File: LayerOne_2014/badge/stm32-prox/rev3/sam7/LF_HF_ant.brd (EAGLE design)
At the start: 99 x 50 mm, 26 parts

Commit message: 
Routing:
- net N$4: track 123.8 -> 138.2 mm
- net LO2: track 54.7 -> 67.1 mm
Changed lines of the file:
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@@
 <layer number="17" name="Pads" color="2" fill="1" visible="yes" active="yes"/>
 <layer number="18" name="Vias" color="2" fill="1" visible="yes" active="yes"/>
-<layer number="19" name="Unrouted" color="6" fill="1" visible="no" active="yes"/>
+<layer number="19" name="Unrouted" color="6" fill="1" visible="yes" active="yes"/>
 <layer number="20" name="Dimension" color="15" fill="1" visible="yes" active="yes"/>
 <layer number="21" name="tPlace" color="7" fill="1" visible="yes" active="yes"/>
@@
 <contactref element="USB1" pad="2"/>
 <wire x1="31.456" y1="9.652" x2="31.536" y2="9.572" width="0.8128" layer="1"/>
-<wire x1="31.536" y1="9.572" x2="31.536" y2="6.652" width="0.8128" layer="1"/>
+<wire x1="31.536" y1="9.572" x2="31.536" y2="6.652" width="1.2192" layer="1"/>
 <wire x1="18.272" y1="12.432" x2="18.288" y2="12.416" width="0.8128" layer="1"/>
 <wire x1="18.288" y1="12.416" x2="18.288" y2="11.938" width="0.8128" layer="1"/>
@@
 <wire x1="21.288" y1="6.652" x2="31.536" y2="6.652" width="0.8128" layer="1"/>
 <wire x1="31.536" y1="12.462" x2="31.456" y2="12.382" width="0.8128" layer="1"/>
-<wire x1="31.456" y1="12.382" x2="31.456" y2="9.652" width="0.8128" layer="1"/>
+<wire x1="31.456" y1="12.382" x2="31.456" y2="9.652" width="1.2192" layer="1"/>
 <wire x1="6.604" y1="17.78" x2="8.382" y2="19.558" width="0.8128" layer="1"/>
 <wire x1="8.382" y1="19.558" x2="15.748" y2="19.558" width="0.8128" layer="1"/>
@@
 <wire x1="18.288" y1="17.018" x2="18.288" y2="11.938" width="0.8128" layer="1"/>
 <wire x1="31.536" y1="6.652" x2="31.496" y2="6.612" width="0.8128" layer="1"/>
-<wire x1="31.496" y1="6.612" x2="31.496" y2="5.08" width="0.8128" layer="1"/>
-<wire x1="31.496" y1="5.08" x2="32.034" y2="4.542" width="0.8128" layer="1"/>
-<wire x1="32.034" y1="4.542" x2="38.716" y2="4.542" width="0.8128" layer="1"/>
+<wire x1="31.496" y1="6.612" x2="31.496" y2="5.08" width="1.2192" layer="1"/>
+<wire x1="31.496" y1="5.08" x2="32.034" y2="4.542" width="1.2192" layer="1"/>
+<wire x1="32.034" y1="4.542" x2="38.716" y2="4.542" width="1.2192" layer="1"/>
 <wire x1="8.128" y1="3.556" x2="12.954" y2="-1.27" width="0.8128" layer="1"/>
 <wire x1="12.954" y1="-1.27" x2="12.954" y2="-4.826" width="0.8128" layer="1"/>
@@
 <contactref element="USB1" pad="1"/>
 <wire x1="31.456" y1="21.272" x2="31.536" y2="21.192" width="0.8128" layer="1"/>
-<wire x1="31.536" y1="21.192" x2="31.536" y2="18.272" width="0.8128" layer="1"/>
+<wire x1="31.536" y1="21.192" x2="31.536" y2="18.272" width="1.2192" layer="1"/>
 <wire x1="31.536" y1="18.272" x2="31.456" y2="18.192" width="0.8128" layer="1"/>
-<wire x1="31.456" y1="18.192" x2="31.456" y2="15.462" width="0.8128" layer="1"/>
+<wire x1="31.456" y1="18.192" x2="31.456" y2="15.462" width="1.2192" layer="1"/>
 <wire x1="31.456" y1="21.272" x2="31.266" y2="21.082" width="0.8128" layer="1"/>
-<wire x1="31.266" y1="21.082" x2="23.622" y2="21.082" width="0.8128" layer="1"/>
-<wire x1="23.622" y1="21.082" x2="20.772" y2="18.232" width="0.8128" layer="1"/>
-<wire x1="20.772" y1="18.232" x2="20.772" y2="18.034" width="0.8128" layer="1"/>
 <wire x1="20.772" y1="18.034" x2="20.772" y2="12.432" width="0.8128" layer="1"/>
 <wire x1="4.191" y1="7.051040625" x2="4.064" y2="7.178040625" width="0.8128" layer="16"/>
@@
 <wire x1="15.748" y1="21.844" x2="16.962" y2="21.844" width="0.8128" layer="1"/>
 <wire x1="16.962" y1="21.844" x2="20.772" y2="18.034" width="0.8128" layer="1"/>
+<wire x1="31.266" y1="21.082" x2="29.972" y2="21.082" width="0.8128" layer="1"/>
+<wire x1="29.972" y1="21.082" x2="28.194" y2="19.304" width="0.8128" layer="1"/>
+<wire x1="28.194" y1="19.304" x2="28.194" y2="12.954" width="0.8128" layer="1"/>
+<wire x1="28.194" y1="12.954" x2="28.194" y2="12.446" width="0.8128" layer="1"/>
+<wire x1="20.772" y1="12.432" x2="20.772" y2="9.962" width="0.8128" layer="1"/>
+<wire x1="20.772" y1="9.962" x2="21.59" y2="9.144" width="0.8128" layer="1"/>
+<wire x1="21.59" y1="9.144" x2="27.432" y2="9.144" width="0.8128" layer="1"/>
+<wire x1="27.432" y1="9.144" x2="28.194" y2="9.906" width="0.8128" layer="1"/>
+<wire x1="28.194" y1="9.906" x2="28.194" y2="12.954" width="0.8128" layer="1"/>
 </signal>
 <signal name="N$3">
@@
 <wire x1="34.336" y1="6.652" x2="34.336" y2="6.002" width="0.4064" layer="1"/>
 <wire x1="34.256" y1="15.462" x2="34.416" y2="15.622" width="0.8128" layer="1"/>
-<wire x1="34.416" y1="15.622" x2="38.716" y2="15.622" width="0.8128" layer="1"/>
+<wire x1="34.416" y1="15.622" x2="38.716" y2="15.622" width="1.2192" layer="1"/>
 <wire x1="34.336" y1="12.462" x2="34.256" y2="12.382" width="0.8128" layer="1"/>
-<wire x1="34.256" y1="12.382" x2="34.256" y2="9.652" width="0.8128" layer="1"/>
+<wire x1="34.256" y1="12.382" x2="34.256" y2="9.652" width="1.2192" layer="1"/>
 <wire x1="34.256" y1="9.652" x2="34.336" y2="9.572" width="0.8128" layer="1"/>
-<wire x1="34.336" y1="9.572" x2="34.336" y2="6.652" width="0.8128" layer="1"/>
+<wire x1="34.336" y1="9.572" x2="34.336" y2="6.652" width="1.2192" layer="1"/>
 <wire x1="34.256" y1="21.272" x2="34.336" y2="21.192" width="0.8128" layer="1"/>
-<wire x1="34.336" y1="21.192" x2="34.336" y2="18.272" width="0.8128" layer="1"/>
+<wire x1="34.336" y1="21.192" x2="34.336" y2="18.272" width="1.2192" layer="1"/>
 <wire x1="34.336" y1="18.272" x2="34.256" y2="18.192" width="0.8128" layer="1"/>
-<wire x1="34.256" y1="18.192" x2="34.256" y2="15.462" width="0.8128" layer="1"/>
+<wire x1="34.256" y1="18.192" x2="34.256" y2="15.462" width="1.2192" layer="1"/>
 <wire x1="34.256" y1="15.462" x2="34.336" y2="15.382" width="0.8128" layer="1"/>
-<wire x1="34.336" y1="15.382" x2="34.336" y2="12.462" width="0.8128" layer="1"/>
+<wire x1="34.336" y1="15.382" x2="34.336" y2="12.462" width="1.2192" layer="1"/>
 </signal>
 <signal name="N$4">
@@
 <contactref element="USB1" pad="4"/>
 <contactref element="JP1" pad="1"/>
-<wire x1="77.398" y1="-3.4" x2="80.398" y2="-3.4" width="0.8128" layer="1"/>
-<wire x1="80.398" y1="-3.4" x2="80.398" y2="-6.6" width="0.8128" layer="1"/>
-<wire x1="80.398" y1="-6.6" x2="77.398" y2="-6.6" width="0.8128" layer="1"/>
+<wire x1="77.398" y1="-3.4" x2="80.398" y2="-3.4" width="1.2192" layer="1"/>
+<wire x1="80.398" y1="-3.4" x2="80.398" y2="-6.6" width="1.2192" layer="1"/>
+<wire x1="80.398" y1="-6.6" x2="77.398" y2="-6.6" width="1.2192" layer="1"/>
 <wire x1="77.3" y1="-3.302" x2="77.398" y2="-3.4" width="0.8128" layer="1"/>
-<wire x1="9.144" y1="-3.048" x2="13.716" y2="1.524" width="0.8128" layer="16"/>
-<via x="13.716" y="1.524" extent="1-16" drill="0.5"/>
-<wire x1="13.716" y1="1.524" x2="13.772" y2="1.58" width="0.8128" layer="1"/>
 <wire x1="85.948" y1="-15" x2="85.934" y2="-14.986" width="0.6096" layer="1"/>
 <wire x1="78.5" y1="-15" x2="85.948" y2="-15" width="0.6096" layer="1"/>
-<wire x1="13.772" y1="12.432" x2="13.716" y2="12.376" width="0.8128" layer="1"/>
-<wire x1="13.716" y1="12.376" x2="13.716" y2="1.524" width="0.8128" layer="1"/>
 <wire x1="13.772" y1="1.58" x2="30.338" y2="-14.986" width="0.8128" layer="1"/>
 <wire x1="30.338" y1="-14.986" x2="64.262" y2="-14.986" width="0.8128" layer="1"/>
@@
 <wire x1="78.5" y1="-15" x2="64.276" y2="-15" width="0.6096" layer="1"/>
 <wire x1="64.276" y1="-15" x2="64.262" y2="-14.986" width="0.7112" layer="1" curve="-90"/>
+<wire x1="13.772" y1="1.58" x2="13.772" y2="12.432" width="0.8128" layer="1"/>
+<wire x1="9.144" y1="-3.048" x2="9.144" y2="0" width="0.8128" layer="16"/>
+<wire x1="9.144" y1="0" x2="11.43" y2="2.286" width="0.8128" layer="16"/>
+<wire x1="11.43" y1="2.286" x2="11.43" y2="10.922" width="0.8128" layer="16"/>
+<wire x1="11.43" y1="10.922" x2="11.43" y2="11.938" width="0.8128" layer="16"/>
+<wire x1="11.43" y1="11.938" x2="13.716" y2="14.224" width="0.8128" layer="16"/>
+<via x="13.716" y="14.224" extent="1-16" drill="0.5"/>
+<wire x1="13.716" y1="14.224" x2="13.772" y2="14.168" width="0.8128" layer="1"/>
+<wire x1="13.772" y1="14.168" x2="13.772" y2="12.432" width="0.8128" layer="1"/>
 </signal>
 <signal name="HF2">
@@
 <contactref element="TP8" pad="TP"/>
 <wire x1="83.598" y1="-9.4" x2="83.998" y2="-9" width="0.4064" layer="1"/>
-<wire x1="77.398" y1="-9.4" x2="80.398" y2="-9.4" width="0.8128" layer="1"/>
+<wire x1="77.398" y1="-9.4" x2="80.398" y2="-9.4" width="1.2192" layer="1"/>
 <wire x1="80.398" y1="-9.4" x2="83.598" y2="-9.4" width="0.8128" layer="1"/>
 <wire x1="83.598" y1="-9.4" x2="83.998" y2="-9" width="0.8128" layer="1"/>
-<wire x1="83.998" y1="-9" x2="83.998" y2="-12" width="0.8128" layer="1"/>
-<wire x1="83.998" y1="-9" x2="83.998" y2="-5.4" width="0.8128" layer="1"/>
-<wire x1="83.998" y1="-5.4" x2="84.398" y2="-5" width="0.8128" layer="1"/>
+<wire x1="83.998" y1="-9" x2="83.998" y2="-12" width="1.2192" layer="1"/>
+<wire x1="83.998" y1="-9" x2="83.998" y2="-5.4" width="1.2192" layer="1"/>
+<wire x1="83.998" y1="-5.4" x2="84.398" y2="-5" width="1.2192" layer="1"/>
 </signal>
 <signal name="N$5">
@@
 <contactref element="C9" pad="1"/>
 <contactref element="JP1" pad="2"/>
-<wire x1="86.798" y1="-9" x2="86.798" y2="-12" width="0.8128" layer="1"/>
+<wire x1="86.798" y1="-9" x2="86.798" y2="-12" width="1.2192" layer="1"/>
 <wire x1="86.848" y1="-15" x2="86.868" y2="-15" width="0.4064" layer="1"/>
 <wire x1="86.868" y1="-15" x2="86.868" y2="-12.7" width="0.6096" layer="1"/>
@@
 <contactref element="TP7" pad="TP"/>
 <contactref element="USB1" pad="3"/>
-<wire x1="77.398" y1="-0.6" x2="80.398" y2="-0.6" width="0.8128" layer="1"/>
-<wire x1="80.398" y1="-0.6" x2="83.998" y2="-0.6" width="0.8128" layer="1"/>
-<wire x1="83.998" y1="-0.6" x2="84.398" y2="-1" width="0.8128" layer="1"/>
+<wire x1="77.398" y1="-0.6" x2="80.398" y2="-0.6" width="1.2192" layer="1"/>
+<wire x1="80.398" y1="-0.6" x2="83.998" y2="-0.6" width="1.2192" layer="1"/>
+<wire x1="83.998" y1="-0.6" x2="84.398" y2="-1" width="1.2192" layer="1"/>
 <wire x1="77.306" y1="-0.508" x2="77.398" y2="-0.6" width="0.8128" layer="1"/>
 <wire x1="9.144" y1="7.051040625" x2="9.144" y2="11.938" width="0.8128" layer="16"/>

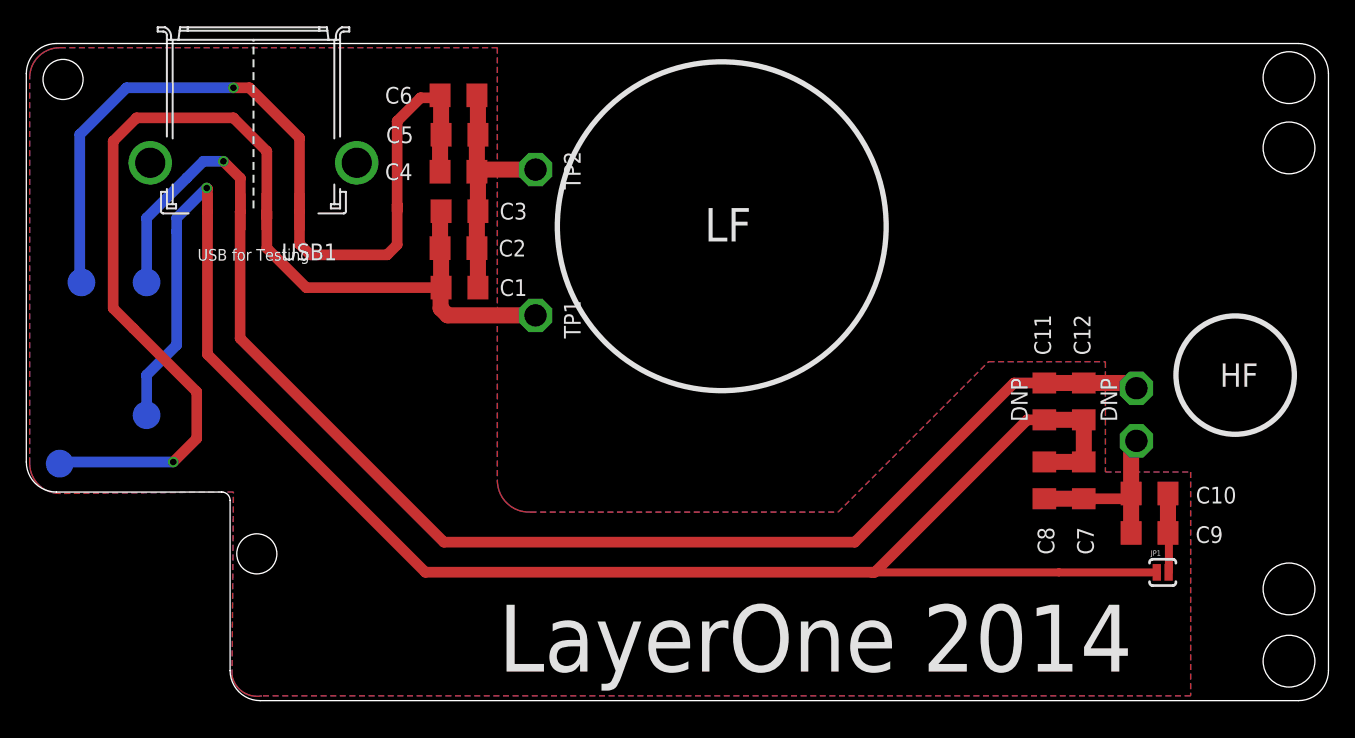
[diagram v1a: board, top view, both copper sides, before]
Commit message: 
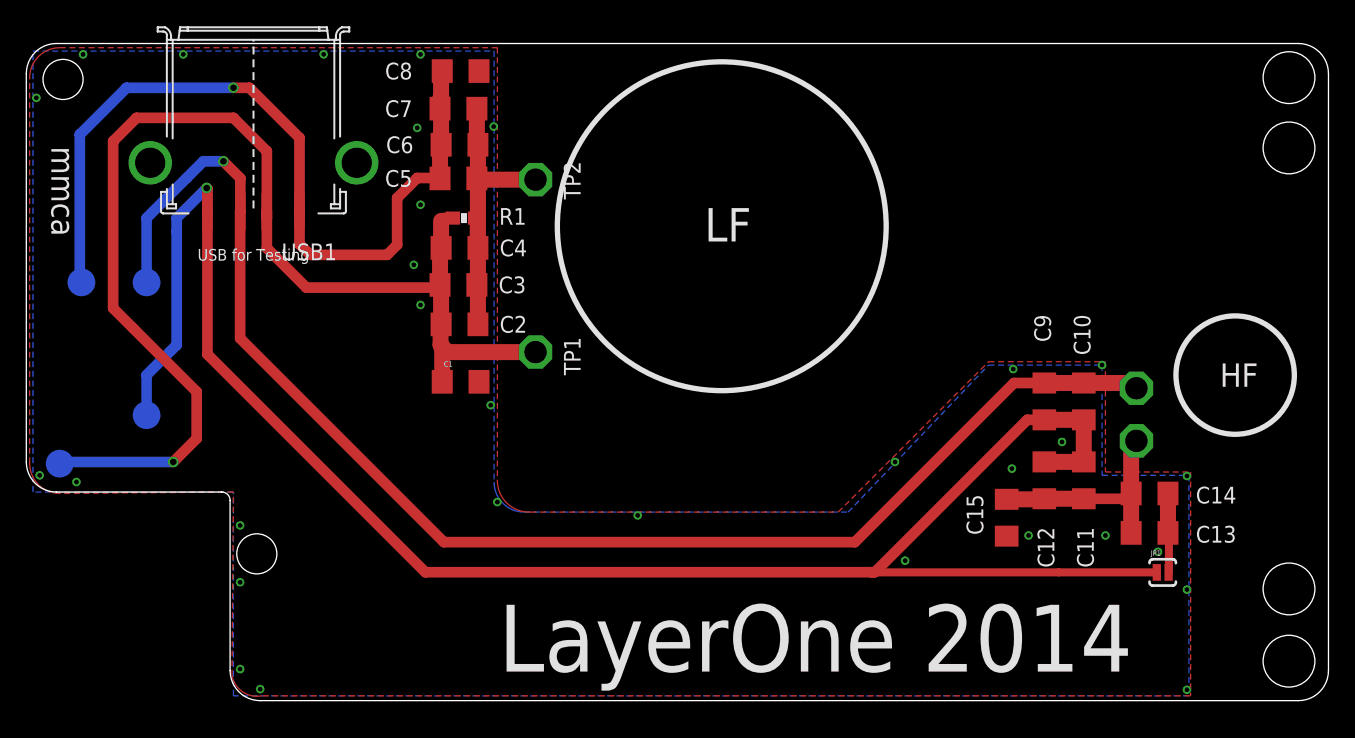
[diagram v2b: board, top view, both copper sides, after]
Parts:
- added C13, C14, C15: (no value), rcl:C1206
- added R1: (no value), SparkFun-Passives:0603-RES
- C10, C9: value (none) -> DNP
- C11, C12: value DNP -> (none)
- C7, C8: device rcl:C1206 -> SparkFun-Passives:1206
- moved C7 55.3 mm to (32.9, 20.3), turned to 0 degrees
- moved C8 54.2 mm to (33.0, 23.1), turned to 0 degrees
- moved C9 12.8 mm to (77.4, -2.00), turned to 270 degrees
- moved C10 8.60 mm to (80.4, -2.00), turned to 270 degrees
- moved C1 7.16 mm to (33.0, -0.51)
- moved C11 6.71 mm to (80.4, -8.00)
- moved C12 6.71 mm to (77.4, -8.00)
- moved C4 5.79 mm to (32.9, 9.67)
- moved C2 5.79 mm to (32.9, 3.86)
- moved C3 5.60 mm to (32.9, 6.86)
- moved C6 3.76 mm to (32.9, 17.5)
- moved C5 3.32 mm to (32.9, 15.0)
- moved TP1 2.79 mm to (38.7, 1.75)
- moved TP2 0.76 mm to (38.7, 14.9)
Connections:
- new net GND: C1.2, C15.2, C8.2
- net HF1: now also C10.1, C9.1; no longer C11.1, C12.1
- net HF2: now also C11.2, C12.2, C13.2, C14.2, C15.1; no longer C10.2, C7.2, C8.2, C9.2
- net LO1: now also C4.1, R1.2
- net LO2: now also C7.1, C8.1; no longer C4.1
- net N$3: now also C7.2, R1.1; no longer C1.2
- net N$4: now also C10.2, C11.1, C12.1, C9.2; no longer C11.2, C12.2, C7.1, C8.1
- net N$5: now also C13.1, C14.1; no longer C10.1, C9.1
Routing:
- net N$3: track 20.0 -> 28.5 mm
- net LO1: track 87.2 -> 92.9 mm
- net HF2: track 14.5 -> 17.4 mm
- net LO2: track 67.1 -> 66.0 mm
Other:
- board text added: "Many parts do not need to be placed"

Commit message: 
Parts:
- moved C1 0.25 mm to (32.8, -0.51)
- moved C8 0.25 mm to (32.8, 23.1)
- moved C2 0.17 mm to (32.8, 3.86)
- moved C4 0.17 mm to (32.8, 9.67)
- moved C6 0.17 mm to (32.8, 17.5)
- moved C3 0.09 mm to (32.8, 6.86)
- moved C5 0.09 mm to (32.8, 15.0)
- moved C7 0.09 mm to (32.8, 20.3)
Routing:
- net N$3: track 28.5 -> 21.6 mm
- net LO2: track 66.0 -> 63.0 mm
- net LO1: track 92.9 -> 95.4 mm
